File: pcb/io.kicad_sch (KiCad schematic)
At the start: 46 parts, among them J2 JST B24B-PADSS-F, J4 JST B04B-XASK, U17 ESD224DQA, U18 ESD224DQA, U19 ESD224DQA, U20 ESD224DQA

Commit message: Added part numbers for assembly
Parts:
- R7, R8: LCSC (none) -> C17714
- RN13, RN16, RN19, RN22: LCSC (none) -> C29718
- RN14, RN15, RN17, RN18, RN20, RN21, RN23, RN24: LCSC (none) -> C20197
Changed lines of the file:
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@@
+      (effects (font (size 1.27 1.27)) hide)
+    )
+    (property "LCSC" "C20197" (id 4) (at 111.76 161.29 0)
       (effects (font (size 1.27 1.27)) hide)
     )
@@
       (effects (font (size 1.27 1.27)) hide)
     )
+    (property "LCSC" "C29718" (id 4) (at 41.91 97.79 0)
+      (effects (font (size 1.27 1.27)) hide)
+    )
     (pin "1")
     (pin "2")
@@
       (effects (font (size 1.27 1.27)) hide)
     )
+    (property "LCSC" "C20197" (id 4) (at 81.28 129.54 0)
+      (effects (font (size 1.27 1.27)) hide)
+    )
     (pin "1")
     (pin "2")
@@
       (effects (font (size 1.27 1.27)) hide)
     )
+    (property "LCSC" "C20197" (id 4) (at 81.28 67.31 0)
+      (effects (font (size 1.27 1.27)) hide)
+    )
     (pin "1")
     (pin "2")
@@
       (effects (font (size 1.27 1.27)) hide)
     )
+    (property "LCSC" "C17714" (id 4) (at 207.01 62.23 0)
+      (effects (font (size 1.27 1.27)) hide)
+    )
     (pin "1")
     (pin "2")
@@
       (effects (font (size 1.27 1.27)) hide)
     )
+    (property "LCSC" "C29718" (id 4) (at 41.91 129.54 0)
+      (effects (font (size 1.27 1.27)) hide)
+    )
     (pin "1")
     (pin "2")
@@
       (effects (font (size 1.27 1.27)) hide)
     )
+    (property "LCSC" "C17714" (id 4) (at 261.62 49.53 0)
+      (effects (font (size 1.27 1.27)) hide)
+    )
     (pin "1")
     (pin "2")
@@
       (effects (font (size 1.27 1.27)) hide)
     )
+    (property "LCSC" "C20197" (id 4) (at 111.76 67.31 0)
+      (effects (font (size 1.27 1.27)) hide)
+    )
     (pin "1")
     (pin "2")
@@
       (effects (font (size 1.27 1.27)) hide)
     )
+    (property "LCSC" "C20197" (id 4) (at 111.76 129.54 0)
+      (effects (font (size 1.27 1.27)) hide)
+    )
     (pin "1")
     (pin "2")
@@
       (effects (font (size 1.27 1.27)) hide)
     )
+    (property "LCSC" "C20197" (id 4) (at 81.28 97.79 0)
+      (effects (font (size 1.27 1.27)) hide)
+    )
     (pin "1")
     (pin "2")
@@
       (effects (font (size 1.27 1.27)) hide)
     )
+    (property "LCSC" "C29718" (id 4) (at 41.91 67.31 0)
+      (effects (font (size 1.27 1.27)) hide)
+    )
     (pin "1")
     (pin "2")
@@
       (effects (font (size 1.27 1.27)) hide)
     )
+    (property "LCSC" "C29718" (id 4) (at 48.26 161.29 0)
+      (effects (font (size 1.27 1.27)) hide)
+    )
     (pin "1")
     (pin "2")
@@
       (effects (font (size 1.27 1.27)) hide)
     )
+    (property "LCSC" "C20197" (id 4) (at 81.28 161.29 0)
+      (effects (font (size 1.27 1.27)) hide)
+    )
     (pin "1")
     (pin "2")
@@
       (effects (font (size 1.27 1.27)) hide)
     )
+    (property "LCSC" "C20197" (id 4) (at 111.76 97.79 0)
+      (effects (font (size 1.27 1.27)) hide)
+    )

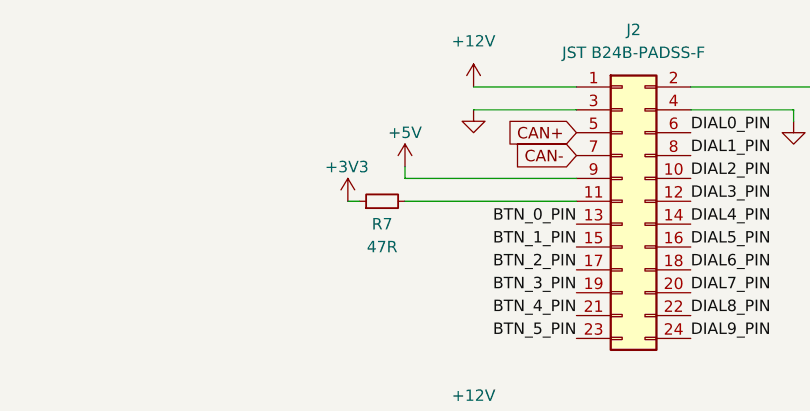
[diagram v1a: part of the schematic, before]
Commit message: Started work on discrete led displays
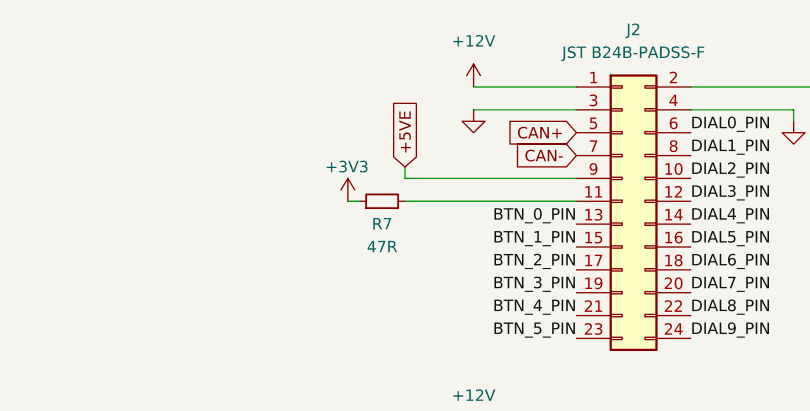
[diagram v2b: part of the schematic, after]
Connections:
- net +5V renamed +5VE
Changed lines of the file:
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@@
+    )
+  )
+  (global_label "+5VE" (shape input) (at 209.55 58.42 90) (fields_autoplaced)
+    (effects (font (size 1.27 1.27)) (justify left))
+    (property "Intersheet References" "${INTERSHEET_REFS}" (id 0) (at 209.4706 50.9874 90)
+      (effects (font (size 1.27 1.27)) (justify left) hide)
     )
   )
@@
     (pin "2")
   )
-  (symbol (lib_id "power:+5V") (at 209.55 58.42 0) (unit 1)
-    (in_bom yes) (on_board yes) (fields_autoplaced)
-    (property "Reference" "#PWR0105" (id 0) (at 209.55 62.23 0)
-      (effects (font (size 1.27 1.27)) hide)
-    )
-    (property "Value" "+5V" (id 1) (at 209.55 54.61 0))
-    (property "Footprint" "" (id 2) (at 209.55 58.42 0)
-      (effects (font (size 1.27 1.27)) hide)
-    )
-    (property "Datasheet" "" (id 3) (at 209.55 58.42 0)
-      (effects (font (size 1.27 1.27)) hide)
-    )
-    (pin "1")
-  )
   (symbol (lib_id "Device:R_Pack04") (at 111.76 67.31 90) (unit 1)
